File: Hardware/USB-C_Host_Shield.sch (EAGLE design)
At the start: 5 parts

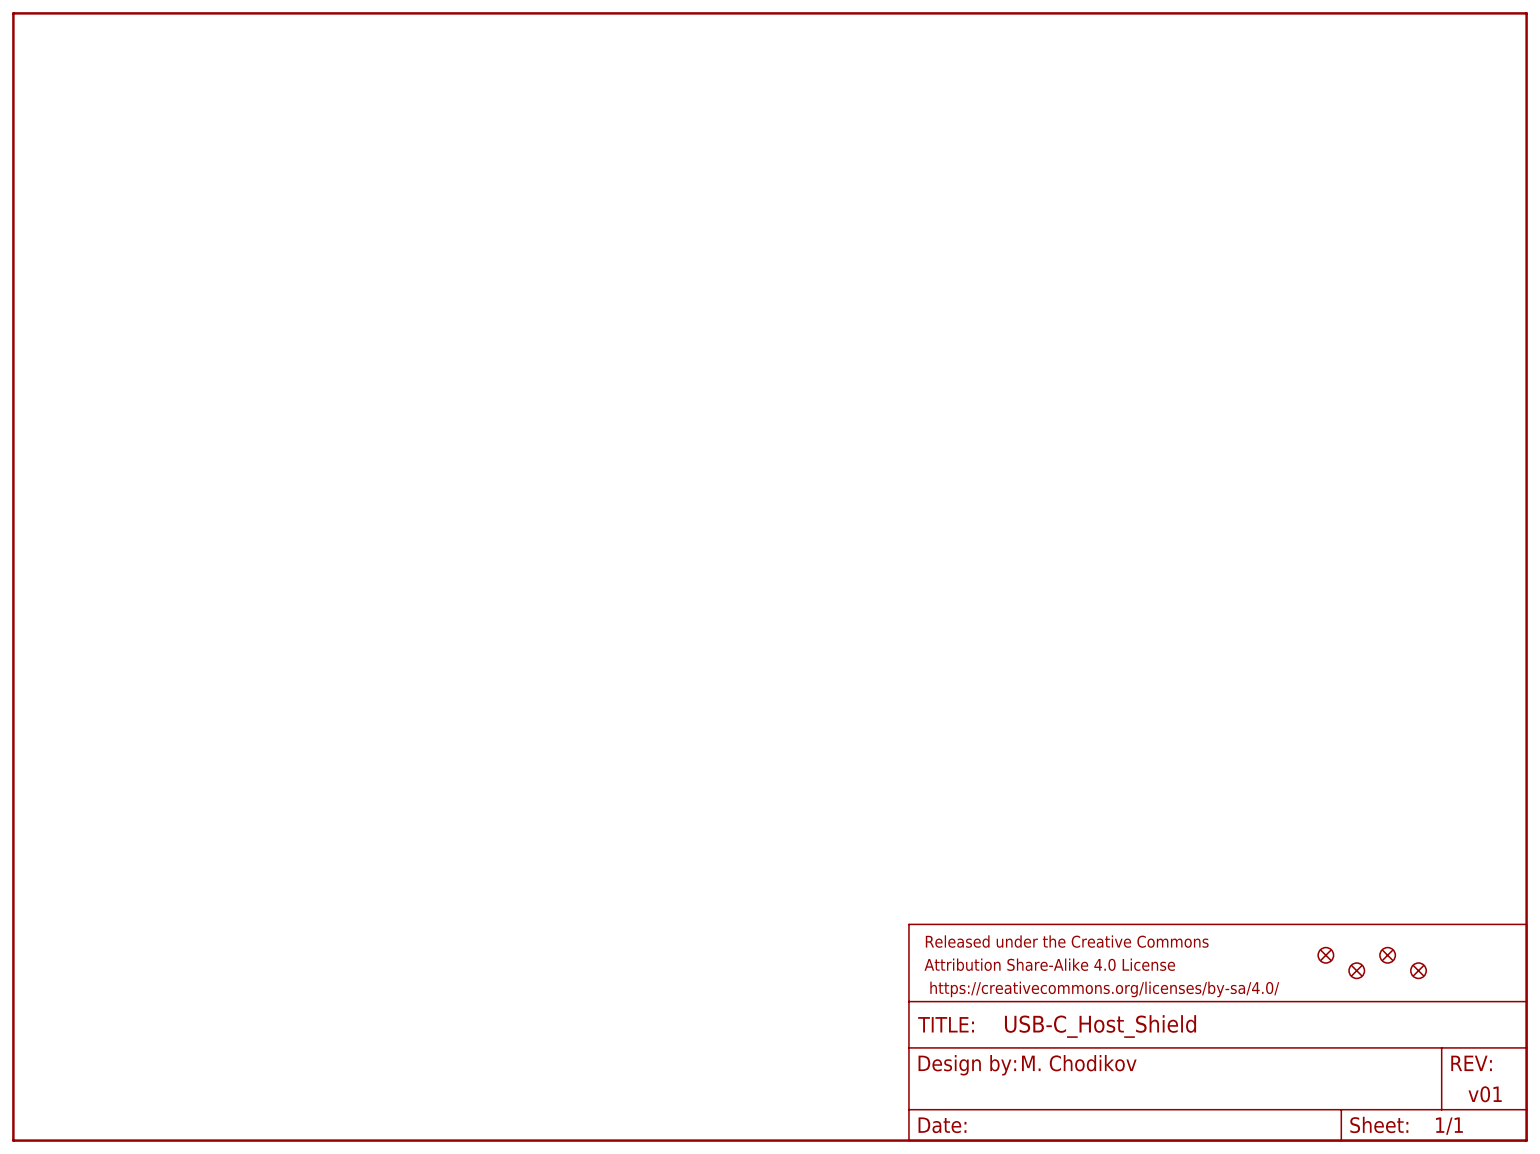
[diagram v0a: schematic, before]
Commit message: Updated schematic
Added initial components
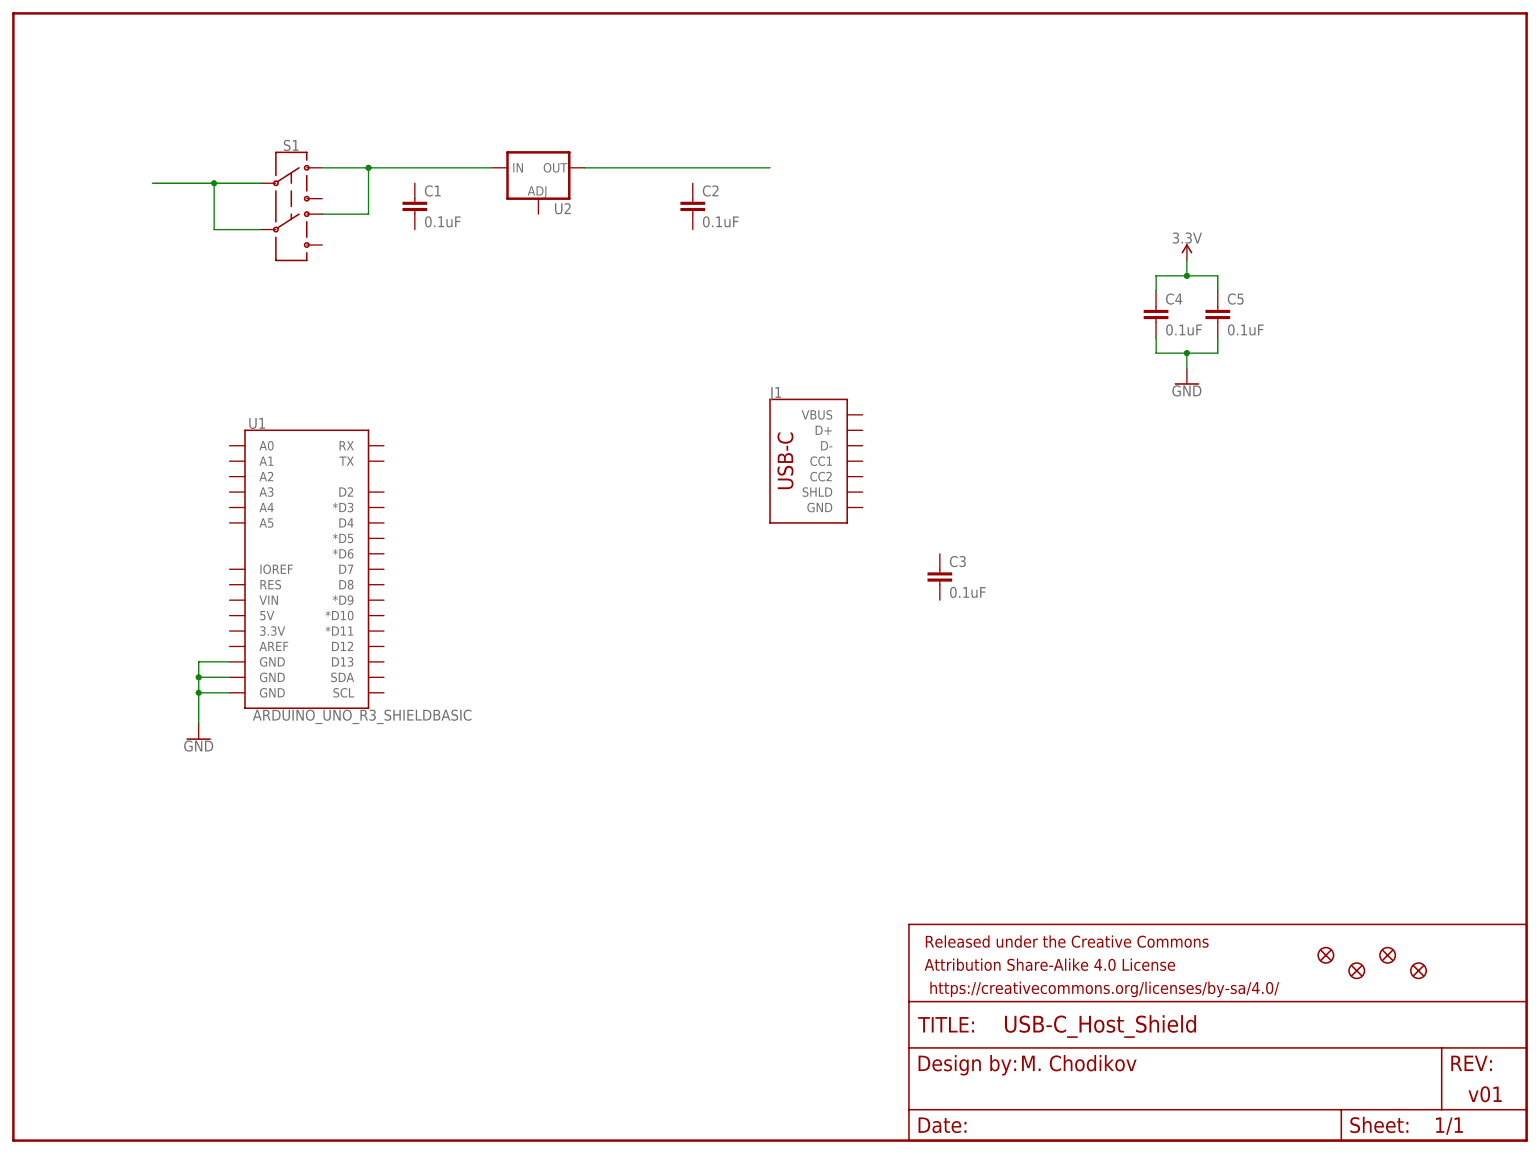
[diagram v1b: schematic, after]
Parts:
- added C1, C2, C3, C4, C5: 0.1uF, SparkFun-Capacitors:0.1UF-0402T-6.3V-10%-X7R
- added J1: (no value), SparkFun-Connectors:USB_C_2-LAYER_PADS
- added S1: (no value), SparkFun-Switches:SWITCH-DPDT-SMD-AYZ0202
- added U1: ARDUINO_UNO_R3_SHIELDBASIC, SparkFun-Boards:ARDUINO_UNO_R3_SHIELDBASIC
- added U2: (no value), SparkFun-IC-Power:V_REG_LM1117SOT223
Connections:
- new net 3.3V: C4.1, C5.1
- new net GND: C4.2, C5.2, U1.GND@0, U1.GND@1, U1.GND@2
- new net N$1: S1.2, S1.5
- new net N$2: S1.3, S1.6, U2.IN
- new net N$3: U2.OUT
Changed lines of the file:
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@@
 <layer number="146" name="DrillLegend_01-20" color="7" fill="1" visible="no" active="no"/>
 <layer number="147" name="PIN_NUMBER" color="7" fill="1" visible="no" active="no"/>
+<layer number="148" name="DrillLegend_01-20" color="7" fill="1" visible="no" active="no"/>
 <layer number="149" name="DrillLegend_02-15" color="7" fill="1" visible="no" active="no"/>
 <layer number="150" name="Notes" color="7" fill="1" visible="no" active="no"/>
@@
 <layer number="154" name="FabDoc2" color="7" fill="1" visible="no" active="no"/>
 <layer number="155" name="FabDoc3" color="7" fill="1" visible="no" active="no"/>
+<layer number="156" name="gesam-Maß" color="7" fill="1" visible="no" active="no"/>
+<layer number="157" name="FaceMchng" color="7" fill="1" visible="no" active="no"/>
+<layer number="158" name="FaceMMeas" color="7" fill="1" visible="no" active="no"/>
+<layer number="159" name="Geh-Bear2" color="7" fill="1" visible="no" active="no"/>
+<layer number="160" name="Topologie" color="7" fill="1" visible="no" active="no"/>
+<layer number="161" name="tomplace2" color="7" fill="1" visible="no" active="no"/>
 <layer number="166" name="AntennaArea" color="7" fill="1" visible="no" active="no"/>
 <layer number="168" name="4mmHeightArea" color="7" fill="1" visible="no" active="no"/>
@@
 <layer number="250" name="Descript" color="3" fill="1" visible="no" active="no"/>
 <layer number="251" name="SMDround" color="12" fill="11" visible="no" active="no"/>
+<layer number="252" name="BR-BS" color="7" fill="1" visible="no" active="no"/>
 <layer number="253" name="Extra" color="7" fill="1" visible="no" active="no"/>
 <layer number="254" name="cooling" color="7" fill="1" visible="no" active="no"/>
@@
 <part name="FD3" library="SparkFun-Aesthetics" deviceset="FIDUCIAL" device="UFIDUCIAL"/>
 <part name="FD4" library="SparkFun-Aesthetics" deviceset="FIDUCIAL" device="UFIDUCIAL"/>
+<part name="U1" library="SparkFun-Boards" deviceset="ARDUINO_UNO_R3_SHIELD" device="BASIC"/>
+<part name="J1" library="SparkFun-Connectors" deviceset="USB_C" device="_2-LAYER_PADS"/>
+<part name="S1" library="SparkFun-Switches" deviceset="SWITCH-DPDT" device="-SMD-AYZ0202"/>
+<part name="U2" library="SparkFun-IC-Power" deviceset="V_REG_LM1117" device="SOT223"/>
+<part name="C1" library="SparkFun-Capacitors" deviceset="0.1UF" device="-0402T-6.3V-10%-X7R" value="0.1uF"/>
+<part name="C2" library="SparkFun-Capacitors" deviceset="0.1UF" device="-0402T-6.3V-10%-X7R" value="0.1uF"/>
+<part name="C3" library="SparkFun-Capacitors" deviceset="0.1UF" device="-0402T-6.3V-10%-X7R" value="0.1uF"/>
+<part name="C4" library="SparkFun-Capacitors" deviceset="0.1UF" device="-0402T-6.3V-10%-X7R" value="0.1uF"/>
+<part name="C5" library="SparkFun-Capacitors" deviceset="0.1UF" device="-0402T-6.3V-10%-X7R" value="0.1uF"/>
+<part name="SUPPLY1" library="SparkFun-PowerSymbols" deviceset="3.3V" device=""/>
+<part name="GND1" library="SparkFun-PowerSymbols" deviceset="GND" device=""/>
+<part name="GND2" library="SparkFun-PowerSymbols" deviceset="GND" device=""/>
 </parts>
 <sheets>
@@
 <instance part="FD3" gate="G$1" x="226.06" y="30.48" smashed="yes"/>
 <instance part="FD4" gate="G$1" x="231.14" y="27.94" smashed="yes"/>
+<instance part="U1" gate="G$1" x="48.26" y="96.52" smashed="yes">
+<attribute name="NAME" x="38.608" y="117.094" size="1.778" layer="95" font="vector"/>
+<attribute name="VALUE" x="39.37" y="70.866" size="1.778" layer="96" font="vector" align="top-left"/>
+</instance>
+<instance part="J1" gate="J1" x="127" y="111.76" smashed="yes">
+<attribute name="VALUE" x="124.46" y="99.314" size="1.778" layer="96" font="vector" rot="MR180" align="top-left"/>
+<attribute name="NAME" x="124.46" y="122.174" size="1.778" layer="95" font="vector"/>
+</instance>
+<instance part="S1" gate="G$1" x="45.72" y="154.94" smashed="yes">
+<attribute name="NAME" x="45.72" y="162.814" size="1.778" layer="95" font="vector" align="bottom-center"/>
+<attribute name="VALUE" x="45.72" y="144.526" size="1.778" layer="96" font="vector" align="top-center"/>
+</instance>
+<instance part="U2" gate="G$1" x="86.36" y="160.02" smashed="yes">
+<attribute name="NAME" x="88.9" y="152.4" size="1.778" layer="95"/>
+<attribute name="VALUE" x="88.9" y="149.86" size="1.778" layer="96"/>
+</instance>
+<instance part="C1" gate="G$1" x="66.04" y="152.4" smashed="yes">
+<attribute name="NAME" x="67.564" y="155.321" size="1.778" layer="95" font="vector"/>
+<attribute name="VALUE" x="67.564" y="150.241" size="1.778" layer="96" font="vector"/>
+</instance>
+<instance part="C2" gate="G$1" x="111.76" y="152.4" smashed="yes">
+<attribute name="NAME" x="113.284" y="155.321" size="1.778" layer="95" font="vector"/>
+<attribute name="VALUE" x="113.284" y="150.241" size="1.778" layer="96" font="vector"/>
+</instance>
+<instance part="C3" gate="G$1" x="152.4" y="91.44" smashed="yes">
+<attribute name="NAME" x="153.924" y="94.361" size="1.778" layer="95" font="vector"/>
+<attribute name="VALUE" x="153.924" y="89.281" size="1.778" layer="96" font="vector"/>
+</instance>
+<instance part="C4" gate="G$1" x="187.96" y="134.62" smashed="yes">
+<attribute name="NAME" x="189.484" y="137.541" size="1.778" layer="95" font="vector"/>
+<attribute name="VALUE" x="189.484" y="132.461" size="1.778" layer="96" font="vector"/>
+</instance>
+<instance part="C5" gate="G$1" x="198.12" y="134.62" smashed="yes">
+<attribute name="NAME" x="199.644" y="137.541" size="1.778" layer="95" font="vector"/>
+<attribute name="VALUE" x="199.644" y="132.461" size="1.778" layer="96" font="vector"/>
+</instance>
+<instance part="SUPPLY1" gate="G$1" x="193.04" y="144.78" smashed="yes">
+<attribute name="VALUE" x="193.04" y="147.574" size="1.778" layer="96" font="vector" align="bottom-center"/>
+</instance>
+<instance part="GND1" gate="1" x="193.04" y="124.46" smashed="yes">
+<attribute name="VALUE" x="193.04" y="124.206" size="1.778" layer="96" font="vector" align="top-center"/>
+</instance>
+<instance part="GND2" gate="1" x="30.48" y="66.04" smashed="yes">
+<attribute name="VALUE" x="30.48" y="65.786" size="1.778" layer="96" font="vector" align="top-center"/>
+</instance>
 </instances>
 <busses>
 </busses>
 <nets>
+<net name="N$1" class="0">
+<segment>
+<pinref part="S1" gate="G$1" pin="2"/>
+<wire x1="40.64" y1="157.48" x2="33.02" y2="157.48" width="0.1524" layer="91"/>
+<pinref part="S1" gate="G$1" pin="5"/>
+<wire x1="40.64" y1="149.86" x2="33.02" y2="149.86" width="0.1524" layer="91"/>
+<wire x1="33.02" y1="149.86" x2="33.02" y2="157.48" width="0.1524" layer="91"/>
+<junction x="33.02" y="157.48"/>
+<wire x1="22.86" y1="157.48" x2="33.02" y2="157.48" width="0.1524" layer="91"/>
+</segment>
+</net>
+<net name="N$2" class="0">
+<segment>
+<pinref part="S1" gate="G$1" pin="6"/>
+<wire x1="50.8" y1="152.4" x2="58.42" y2="152.4" width="0.1524" layer="91"/>
+<wire x1="58.42" y1="152.4" x2="58.42" y2="160.02" width="0.1524" layer="91"/>
+<pinref part="S1" gate="G$1" pin="3"/>
+<wire x1="58.42" y1="160.02" x2="50.8" y2="160.02" width="0.1524" layer="91"/>
+<wire x1="58.42" y1="160.02" x2="78.74" y2="160.02" width="0.1524" layer="91"/>
+<junction x="58.42" y="160.02"/>
+<pinref part="U2" gate="G$1" pin="IN"/>
+</segment>
+</net>
+<net name="N$3" class="0">
+<segment>
+<pinref part="U2" gate="G$1" pin="OUT"/>
+<wire x1="93.98" y1="160.02" x2="124.46" y2="160.02" width="0.1524" layer="91"/>
+</segment>
+</net>
+<net name="3.3V" class="0">
+<segment>
+<pinref part="C4" gate="G$1" pin="1"/>
+<wire x1="187.96" y1="139.7" x2="187.96" y2="142.24" width="0.1524" layer="91"/>
+<wire x1="187.96" y1="142.24" x2="193.04" y2="142.24" width="0.1524" layer="91"/>
+<pinref part="SUPPLY1" gate="G$1" pin="3.3V"/>
+<wire x1="193.04" y1="142.24" x2="193.04" y2="144.78" width="0.1524" layer="91"/>
+<pinref part="C5" gate="G$1" pin="1"/>
+<wire x1="193.04" y1="142.24" x2="198.12" y2="142.24" width="0.1524" layer="91"/>
+<wire x1="198.12" y1="142.24" x2="198.12" y2="139.7" width="0.1524" layer="91"/>
+<junction x="193.04" y="142.24"/>
+</segment>
+</net>
+<net name="GND" class="0">
+<segment>
+<pinref part="C4" gate="G$1" pin="2"/>
+<wire x1="187.96" y1="132.08" x2="187.96" y2="129.54" width="0.1524" layer="91"/>
+<wire x1="187.96" y1="129.54" x2="193.04" y2="129.54" width="0.1524" layer="91"/>
+<pinref part="C5" gate="G$1" pin="2"/>
+<wire x1="193.04" y1="129.54" x2="198.12" y2="129.54" width="0.1524" layer="91"/>
+<wire x1="198.12" y1="129.54" x2="198.12" y2="132.08" width="0.1524" layer="91"/>
+<pinref part="GND1" gate="1" pin="GND"/>
+<wire x1="193.04" y1="127" x2="193.04" y2="129.54" width="0.1524" layer="91"/>
+<junction x="193.04" y="129.54"/>
+</segment>
+<segment>
+<pinref part="U1" gate="G$1" pin="GND@2"/>
+<pinref part="GND2" gate="1" pin="GND"/>
+<wire x1="35.56" y1="78.74" x2="30.48" y2="78.74" width="0.1524" layer="91"/>
+<wire x1="30.48" y1="78.74" x2="30.48" y2="76.2" width="0.1524" layer="91"/>
+<pinref part="U1" gate="G$1" pin="GND@1"/>
+<wire x1="30.48" y1="76.2" x2="30.48" y2="73.66" width="0.1524" layer="91"/>
+<wire x1="30.48" y1="73.66" x2="30.48" y2="68.58" width="0.1524" layer="91"/>
+<wire x1="35.56" y1="76.2" x2="30.48" y2="76.2" width="0.1524" layer="91"/>
+<junction x="30.48" y="76.2"/>
+<pinref part="U1" gate="G$1" pin="GND@0"/>
+<wire x1="35.56" y1="73.66" x2="30.48" y2="73.66" width="0.1524" layer="91"/>
+<junction x="30.48" y="73.66"/>
+</segment>
+</net>
 </nets>
 </sheet>

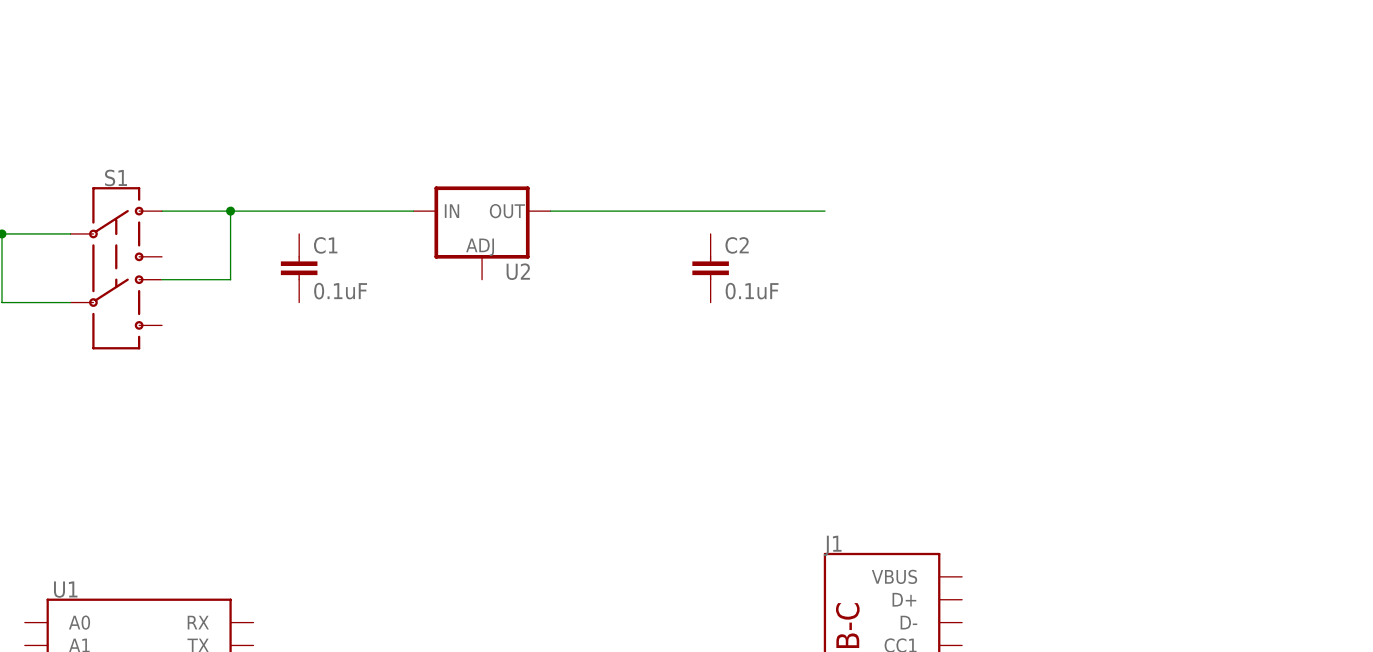
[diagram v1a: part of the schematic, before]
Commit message: Updates to schematic, added datasheets
Continued work on the schematic, and added the 3 datasheets for the 3 used IC's on the board for power and data processing.
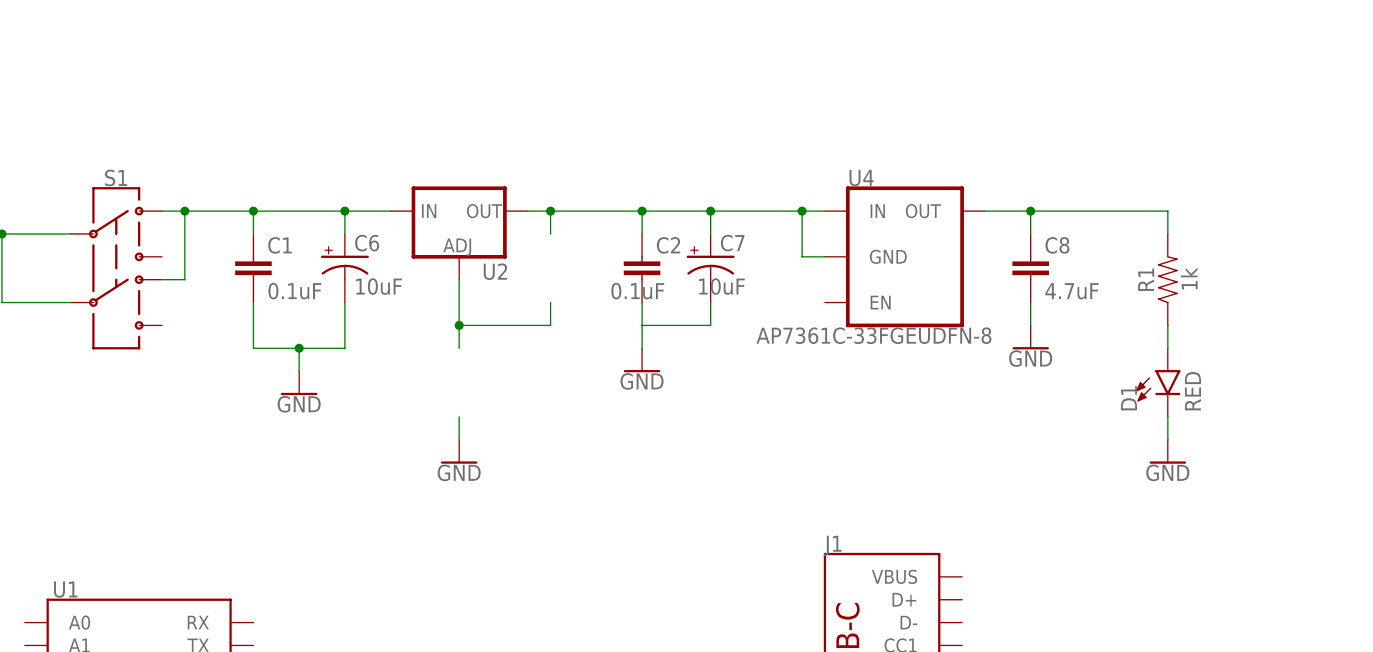
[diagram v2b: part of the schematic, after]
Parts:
- added C6, C7: 10uF, SparkFun-Capacitors:10UF-POLAR-EIA3216-16V-10%(TANT)
- added C8: 4.7uF, SparkFun-Capacitors:4.7UF-0603-6.3V-(10%)
- added D1: RED, SparkFun-LED:LED-RED0603
- added R1: 1k, SparkFun-Resistors:1KOHM-0603-1/10W-1%
- added U4: AP7361C-33FGEUDFN-8, SparkFun-IC-Power:AP7361C-33FGEUDFN-8
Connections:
- new net N$4: U2.ADJ
- new net N$6: C2.2, C7.-
- new net N$7: D1.A, R1.1
- new net N$8: D1.C
- new net N$9: C8.1, R1.2, U4.OUT
- net GND: now also C1.2, C6.-, C8.2
- net N$2: now also C1.1, C6.+
- net N$3: now also C2.1, C7.+, U4.GND, U4.IN
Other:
- moved on the sheet: C1, C2, U2
